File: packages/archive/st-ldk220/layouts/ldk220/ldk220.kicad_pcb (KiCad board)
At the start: 2 copper layers, 5 parts

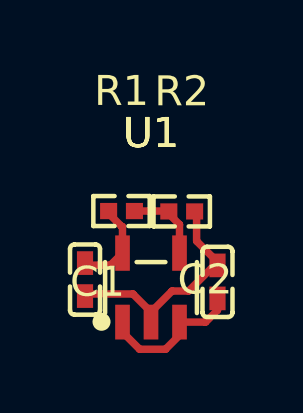
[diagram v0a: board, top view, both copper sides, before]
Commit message: fix button 3d model
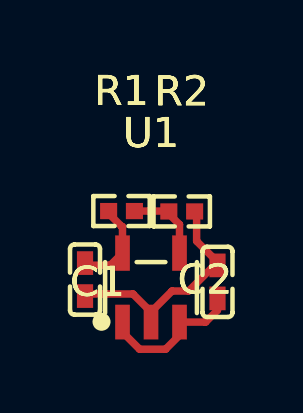
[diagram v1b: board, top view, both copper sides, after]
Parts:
- U1: footprint ST_LDK220M_R:SOT-23-5_L3.0-W1.7-P0.95-LS2.8-BL -> STMicroelectronics_LDK220M_R:SOT-23-5_L3.0-W1.7-P0.95-LS2.8-BL
